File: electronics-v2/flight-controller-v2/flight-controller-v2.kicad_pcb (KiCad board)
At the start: 4 copper layers, 45 x 89 mm, 115 parts, among them J1 Conn_01x02, J10 Conn_01x05, J11 Conn_01x06, J12 Conn_02x03_Odd_Even, J2 Conn_01x03, J3 Conn_01x03, J4 Conn_01x03, J5 Conn_01x03, J6 Conn_01x03, J7 Conn_01x02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

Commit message: fixes in routing
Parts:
- J10: value Conn_01x05 -> Conn_01x06; footprint goose:tht_pin_01x05 -> goose:tht_pin_01x06
- J11: value Conn_01x06 -> Conn_02x03_Odd_Even; footprint goose:tht_pin_01x06 -> Connector_IDC:IDC-Header_2x03_P2.54mm_Vertical
- J12: value Conn_02x03_Odd_Even -> Conn_01x05; footprint Connector_IDC:IDC-Header_2x03_P2.54mm_Vertical -> goose:tht_pin_01x05
- J9: value Conn_01x05 -> Conn_02x04_Odd_Even; footprint goose:tht_pin_01x05 -> goose:tht_pin_02x04
- moved J12 60.6 mm to (149.9, 80.2), turned to -90 degrees
- moved J11 42.2 mm to (129.2, 137.2), turned to 90 degrees
- moved G*** 41.9 mm to (131.0, 120.7)
- moved G*** 34.1 mm to (152.4, 111.3)
- moved J10 12.0 mm to (147.3, 77.7), turned to -90 degrees
- moved G*** 8.25 mm to (147.5, 130.8)
- moved C24 5.51 mm to (145.5, 87.0)
- moved R27 4.03 mm to (150.5, 101.0), turned to 0 degrees
- moved R31 4.00 mm to (145.2, 81.5)
- moved R25 2.75 mm to (155.0, 84.5)
- moved R26 2.75 mm to (155.0, 82.5)
- moved R4 2.02 mm to (155.5, 119.2), turned to 0 degrees
- moved J9 1.29 mm to (139.8, 93.5)
- moved D1 0.35 mm to (157.2, 119.2)
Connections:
- net /power/INT_I2C_SCL renamed /power/SENSOR_I2C_SCL
- net /power/INT_I2C_SDA renamed /power/SENSOR_I2C_SDA
- J10 pad 1: /ucontroller/RESET -> /ucontroller/GPS_PPS
- J10 pad 2: /ucontroller/SWCLK -> +3.3V
- J10 pad 3: /ucontroller/SWDIO -> /ucontroller/GPS_RX
- J10 pad 4: GND -> /ucontroller/GPS_TX
- J10 pad 5: +3.3V -> GND
- J11 pad 1: /ucontroller/PA0 -> /ucontroller/VLX_XSHUT
- J11 pad 2: +3.3V -> /ucontroller/VLX_INT
- J11 pad 3: /ucontroller/UART2_RX -> /ucontroller/VLX_SDA
- J11 pad 4: /ucontroller/UART2_TX -> /ucontroller/VLX_SCL
- J11 pad 6: /ucontroller/PA1 -> +3.3V
- J12 pad 1: /sensors/VLX_XSHUT -> /ucontroller/RESET
- J12 pad 2: /sensors/VLX_INT -> /ucontroller/SWCLK
- J12 pad 3: /sensors/VLX_SDA -> /ucontroller/SWDIO
- J12 pad 4: /sensors/VLX_SCL -> GND
- J12 pad 5: GND -> +3.3V
- J9 pad 1: /ucontroller/SPI3_SCK -> GND
- J9 pad 3: /ucontroller/SPI3_MISO -> /ucontroller/NRF_CE
- J9 pad 4: /ucontroller/SPI3_MOSI -> /ucontroller/NRF_CSN
- J9 pad 5: GND -> /ucontroller/NRF_SCK
- R18 pad 2: /sensors/VLX_SDA -> /ucontroller/VLX_SDA
- R22 pad 2: /sensors/VLX_SCL -> /ucontroller/VLX_SCL
- U4 pad 14: /ucontroller/PA0 -> /ucontroller/GPS_PPS
- U4 pad 15: /ucontroller/PA1 -> /ucontroller/GPS_EN
- U4 pad 16: /ucontroller/UART2_TX -> /ucontroller/GPS_TX
- U4 pad 17: /ucontroller/UART2_RX -> /ucontroller/GPS_RX
- U4 pad 29: /ucontroller/LED_B -> unconnected-(U4-Pad29)
- U4 pad 33: /ucontroller/LED_G -> /ucontroller/LED_B
- U4 pad 34: /ucontroller/LED_R -> /ucontroller/LED_G
- U4 pad 35: unconnected-(U4-Pad35) -> /ucontroller/LED_R
- U4 pad 39: /sensors/VLX_XSHUT -> /ucontroller/VLX_XSHUT
- U4 pad 40: /sensors/VLX_SDA -> /ucontroller/VLX_SDA
- U4 pad 41: /sensors/VLX_SCL -> /ucontroller/VLX_SCL
- U4 pad 42: /power/PWM_ESC -> /ucontroller/VLX_INT
- U4 pad 43: /sensors/VLX_INT -> /power/PWM_ESC
- U4 pad 50: unconnected-(U4-Pad50) -> /sensors/IMU_INT
- U4 pad 51: /ucontroller/SPI3_SCK -> /ucontroller/NRF_SCK
- U4 pad 52: /ucontroller/SPI3_MISO -> /ucontroller/NRF_MISO
- U4 pad 53: /ucontroller/SPI3_MOSI -> /ucontroller/NRF_MOSI
- U4 pad 54: unconnected-(U4-Pad54) -> /ucontroller/NRF_IRQ
- U4 pad 55: unconnected-(U4-Pad55) -> /ucontroller/ESP_UART1_RX
- U4 pad 56: /sensors/IMU_INT -> /ucontroller/NRF_CSN
- U4 pad 57: /sensors/MAG_INT -> /ucontroller/NRF_CE
- U4 pad 59: /ucontroller/ESP_UART1_RX -> /sensors/MAG_INT
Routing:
- net /ucontroller/GPS_PPS: track 0.00 -> 57.6 mm, vias 0 -> 1
- net /ucontroller/GPS_RX: track 0.00 -> 53.8 mm, vias 0 -> 1
- net +3.3V: track 62.2 -> 114.4 mm, vias 46 -> 42
- net /ucontroller/GPS_TX: track 0.00 -> 50.3 mm, vias 0 -> 1
- net /ucontroller/GPS_EN: track 0.00 -> 45.6 mm, vias 0 -> 1
- net /ucontroller/SPI3_SCK: track 40.6 -> 0.00 mm, vias 2 -> 0
- net /ucontroller/VLX_SDA: track 0.00 -> 36.6 mm, vias 0 -> 1
- net /sensors/VLX_SDA: track 36.6 -> 0.00 mm, vias 1 -> 0
- net /ucontroller/PA0: track 35.5 -> 0.00 mm, vias 1 -> 0
- net /ucontroller/SPI3_MISO: track 35.4 -> 0.00 mm, vias 2 -> 0
- net /ucontroller/NRF_SCK: track 0.00 -> 35.2 mm, vias 0 -> 2
- net /ucontroller/VLX_SCL: track 0.00 -> 34.3 mm, vias 0 -> 1
- net /sensors/VLX_SCL: track 34.3 -> 0.00 mm, vias 1 -> 0
- net /ucontroller/NRF_MISO: track 0.00 -> 32.6 mm, vias 0 -> 2
- net /ucontroller/SPI3_MOSI: track 32.2 -> 0.00 mm, vias 2 -> 0
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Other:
- board text added: "CE"
- board text added: "CLK"
- board text added: "CSN"
- board text added: "DIO"
- board text added: "EN"
- board text added: "IRQ"
- board text added: "PPS"
- board text removed: "PA0"
- board text removed: "PA1"

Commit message: more fixes
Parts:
- moved G*** 5.10 mm to (152.5, 129.8)
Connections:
- U2 pad 9: (no net) -> GND
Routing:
- net GND: track 106.5 -> 102.8 mm, vias 96 -> 99
- net /sensors/HALL: track 45.8 -> 43.2 mm
- net /ucontroller/BOOT0: track 29.7 -> 28.3 mm
- net /ucontroller/GPS_PPS: track 57.6 -> 58.4 mm
- net /ucontroller/GPS_EN: track 45.6 -> 46.4 mm
- net /ucontroller/GPS_RX: track 53.8 -> 54.5 mm

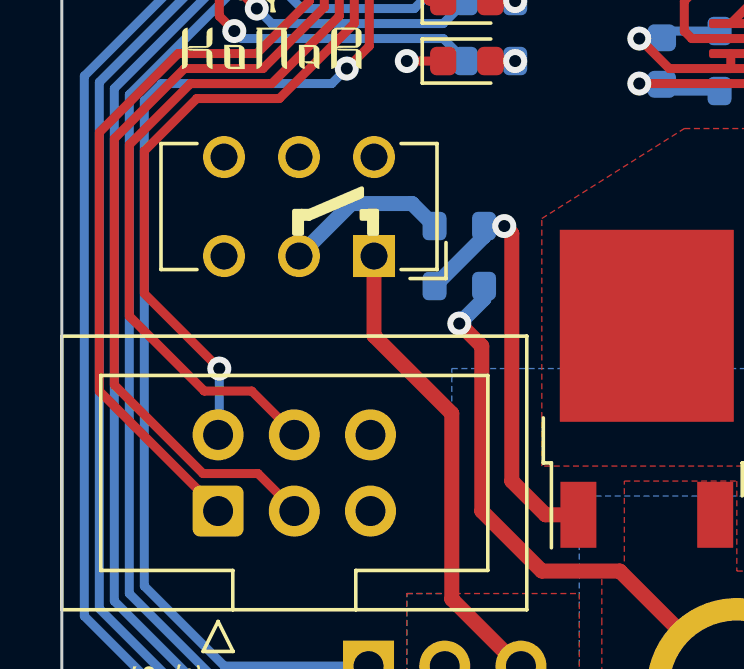
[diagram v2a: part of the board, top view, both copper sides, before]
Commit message: add on/off text near switch
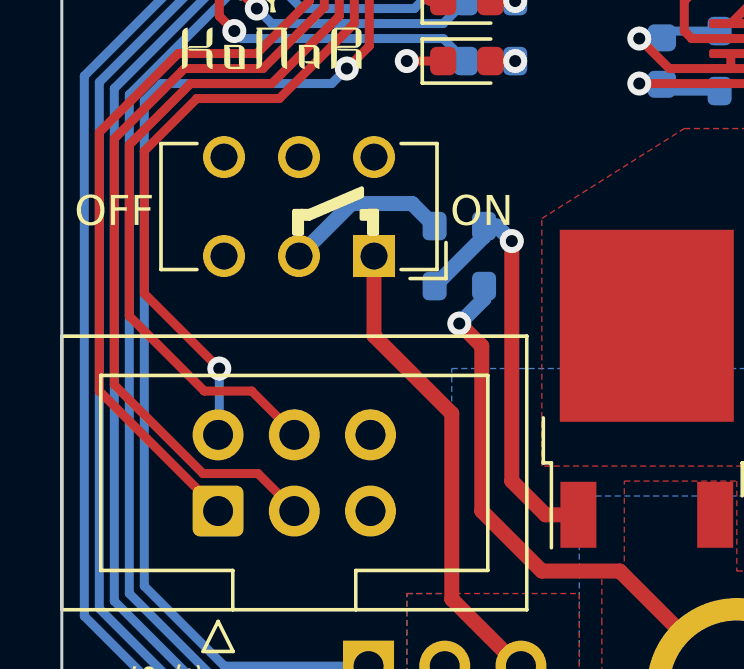
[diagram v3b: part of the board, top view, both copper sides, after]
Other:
- board text added: "OFF"
- board text added: "ON"
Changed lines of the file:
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@@
     )
     (fp_line (start 1.4 1) (end 1.4 -1) (layer "B.SilkS") (width 0.12))
+    (fp_line (start -1.4 -1) (end -1.4 1) (layer "B.SilkS") (width 0.12))
     (fp_line (start -1.4 1) (end 1.4 1) (layer "B.SilkS") (width 0.12))
     (fp_line (start 1.4 -1) (end -1.4 -1) (layer "B.SilkS") (width 0.12))
-    (fp_line (start -1.4 -1) (end -1.4 1) (layer "B.SilkS") (width 0.12))
     (fp_line (start 1.65 -1.25) (end -1.65 -1.25) (layer "B.CrtYd") (width 0.05))
     (fp_line (start 1.65 -1.25) (end 1.65 1.25) (layer "B.CrtYd") (width 0.05))
@@
     (effects (font (size 0.75 0.75) (thickness 0.15)) (justify left))
   )
+  (gr_text "ON" (at 138 127.25) (layer "F.SilkS")
+    (effects (font (size 1 1) (thickness 0.15)))
+  )
   (gr_text "3V3" (at 149 69 90) (layer "F.SilkS")
     (effects (font (size 0.75 0.75) (thickness 0.15)) (justify right))
@@
   (gr_text "JLCJLCJLCJLC" (at 159 92.5 90) (layer "F.SilkS")
     (effects (font (size 1 1) (thickness 0.2)))
+  )
+  (gr_text "OFF" (at 125.75 127.25) (layer "F.SilkS")
+    (effects (font (size 1 1) (thickness 0.15)))
   )
   (gr_text "BOOT" (at 133.75 89.69) (layer "F.SilkS")
@@
   (segment (start 133.5 122.5) (end 133 123) (width 0.3) (layer "B.Cu") (net 50))
   (segment (start 133 123) (end 127.325712 123) (width 0.3) (layer "B.Cu") (net 50))
-  (segment (start 139 128) (end 139 136.25) (width 0.5) (layer "F.Cu") (net 54))
   (segment (start 139 136.25) (end 140.125 137.375) (width 0.5) (layer "F.Cu") (net 54))
   (segment (start 140.125 137.375) (end 141.22 137.375) (width 0.5) (layer "F.Cu") (net 54))
-  (segment (start 138.75 127.75) (end 139 128) (width 0.5) (layer "F.Cu") (net 54))
-  (via (at 138.75 127.75) (size 0.8) (drill 0.4) (layers "F.Cu" "B.Cu") (net 54))
-  (segment (start 138.075 127.75) (end 138.75 127.75) (width 0.5) (layer "B.Cu") (net 54))
+  (segment (start 139 128.25) (end 139 136.25) (width 0.5) (layer "F.Cu") (net 54))
+  (via (at 139 128.25) (size 0.8) (drill 0.4) (layers "F.Cu" "B.Cu") (net 54))
   (segment (start 138.075 127.75) (end 138.075 128.1) (width 0.5) (layer "B.Cu") (net 54))
   (segment (start 138.075 128.1) (end 136.425 129.75) (width 0.5) (layer "B.Cu") (net 54))
+  (segment (start 138.5 127.75) (end 139 128.25) (width 0.5) (layer "B.Cu") (net 54))
+  (segment (start 138.075 127.75) (end 138.5 127.75) (width 0.5) (layer "B.Cu") (net 54))
   (segment (start 148.5375 123.5375) (end 148.25 123.25) (width 0.3) (layer "F.Cu") (net 55))
   (segment (start 148.5375 125.675) (end 148.5375 123.5375) (width 0.3) (layer "F.Cu") (net 55))

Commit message: fix route name, remove ADC code
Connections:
- U2 pad 9: GND -> (no net)
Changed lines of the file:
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@@
     (pad "8" smd roundrect (at 2.48 -1.905 180) (size 1.94 0.6) (layers "F.Cu" "F.Paste" "F.Mask") (roundrect_rratio 0.25)
       (net 16 "/power/BST") (pinfunction "BST") (pintype "passive"))
-    (pad "9" thru_hole circle (at 0.7 -1 180) (size 0.5 0.5) (drill 0.2) (layers *.Cu)
-      (net 2 "GND"))
-    (pad "9" thru_hole circle (at -0.7 0 180) (size 0.5 0.5) (drill 0.2) (layers *.Cu)
-      (net 2 "GND"))
-    (pad "9" thru_hole circle (at -0.7 1 180) (size 0.5 0.5) (drill 0.2) (layers *.Cu)
-      (net 2 "GND"))
-    (pad "9" thru_hole circle (at 0.7 1 180) (size 0.5 0.5) (drill 0.2) (layers *.Cu)
-      (net 2 "GND"))
-    (pad "9" thru_hole circle (at 0.7 0 180) (size 0.5 0.5) (drill 0.2) (layers *.Cu)
-      (net 2 "GND"))
+    (pad "9" thru_hole circle (at 0.7 -1 180) (size 0.5 0.5) (drill 0.2) (layers *.Cu))
+    (pad "9" thru_hole circle (at -0.7 0 180) (size 0.5 0.5) (drill 0.2) (layers *.Cu))
+    (pad "9" thru_hole circle (at -0.7 1 180) (size 0.5 0.5) (drill 0.2) (layers *.Cu))
+    (pad "9" thru_hole circle (at 0.7 1 180) (size 0.5 0.5) (drill 0.2) (layers *.Cu))
+    (pad "9" thru_hole circle (at 0.7 0 180) (size 0.5 0.5) (drill 0.2) (layers *.Cu))
     (pad "9" smd rect (at 0 0 180) (size 2.62 3.51) (layers "F.Cu" "F.Mask"))
-    (pad "9" thru_hole circle (at -0.7 -1 180) (size 0.5 0.5) (drill 0.2) (layers *.Cu)
-      (net 2 "GND"))
-    (pad "9" smd rect (at 0 0 180) (size 1.9 2.5) (layers "B.Cu")
-      (net 2 "GND"))
+    (pad "9" thru_hole circle (at -0.7 -1 180) (size 0.5 0.5) (drill 0.2) (layers *.Cu))
+    (pad "9" smd rect (at 0 0 180) (size 1.9 2.5) (layers "B.Cu"))
     (model "${KICAD6_3DMODEL_DIR}/Package_SO.3dshapes/SOIC-8-1EP_3.9x4.9mm_P1.27mm_EP2.62x3.51mm.wrl"
       (offset (xyz 0 0 0))
